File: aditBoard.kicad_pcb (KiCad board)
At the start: 4 copper layers, 13.2 x 30 mm, 31 parts, among them J1 USB_C_Receptacle_USB2.0, J2 Hashboard0, U2 W25X40CLUXIG TR, U3 RP2040, U4 AP2112K-3.3TRG1, Y1 12MHz

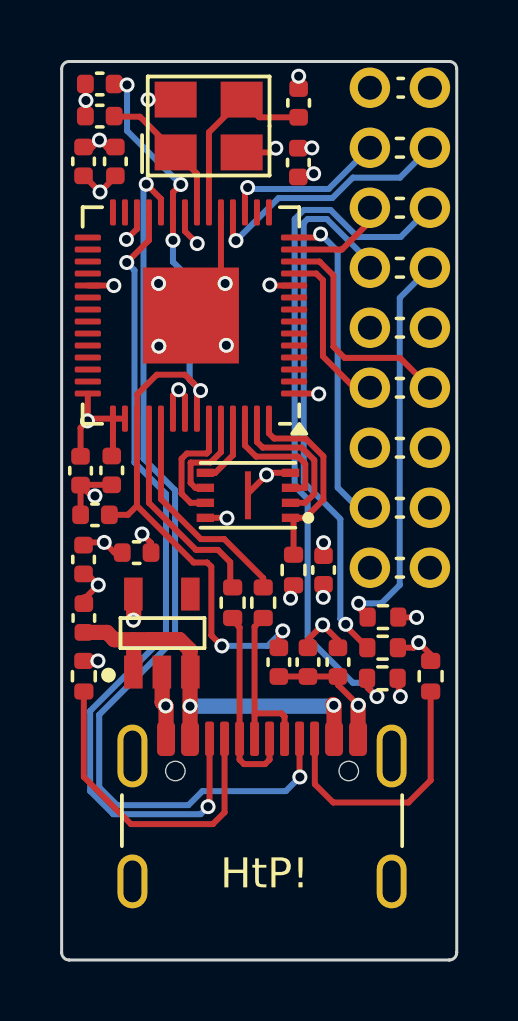
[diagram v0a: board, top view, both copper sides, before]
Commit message: bumped version to 2. added RGB LED
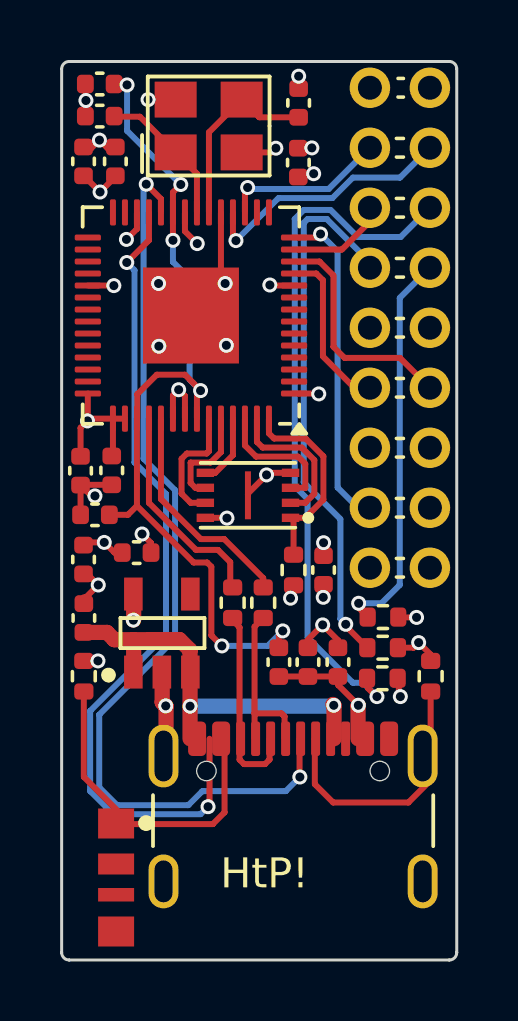
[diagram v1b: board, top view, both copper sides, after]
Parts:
- added U1: SK6812, aditBoard:LED-SMD_4P-L4.0-W1.6-L, F.Cu at (116.2, 108.0)
- U2: value W25X40CLUXIG TR -> W25Q16JVUXIQ
- moved J1 1.03 mm to (122.1, 107.1)
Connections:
- U3 pad 3: unconnected-(U3-GPIO1-Pad3) -> Net-(U1-DIN)
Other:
- copper layers 4 -> 6
- board text added: "v2"
- board text removed: "v1"

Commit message: switched to 6L. Routed LED
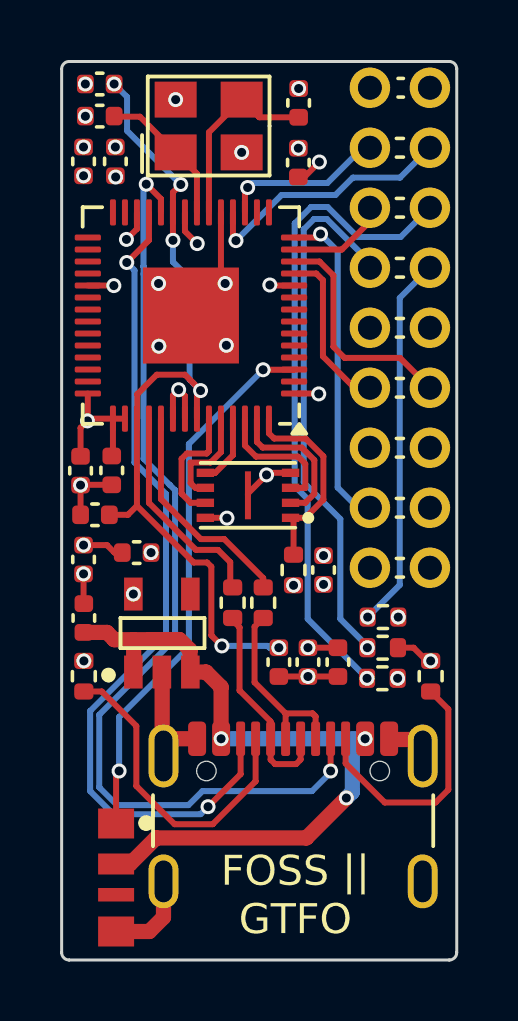
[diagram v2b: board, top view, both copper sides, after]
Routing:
- net Net-(U1-DIN): track 0.00 -> 18.2 mm, vias 0 -> 2
- net /5V: track 13.9 -> 24.3 mm, vias 2 -> 3
- net /GND: track 26.3 -> 19.6 mm, vias 21 -> 22
- net /3V3: track 19.4 -> 16.1 mm, vias 15 -> 16
- net /A2: track 23.4 -> 21.8 mm
- net /1V1: track 29.2 -> 28.0 mm
- net /SWCLK: track 31.4 -> 32.3 mm
- net /A0: track 13.2 -> 12.5 mm
- net Net-(J1-CC2): track 8.90 -> 8.24 mm
- added copper zone on In3.Cu, net /3V3
- added copper zone on In4.Cu, net /GND
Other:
- board text added: "FOSS || GTFO"
- board text removed: "HtP!"

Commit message: Added option for BOOT and RESET buttons. added gerbers and BOM
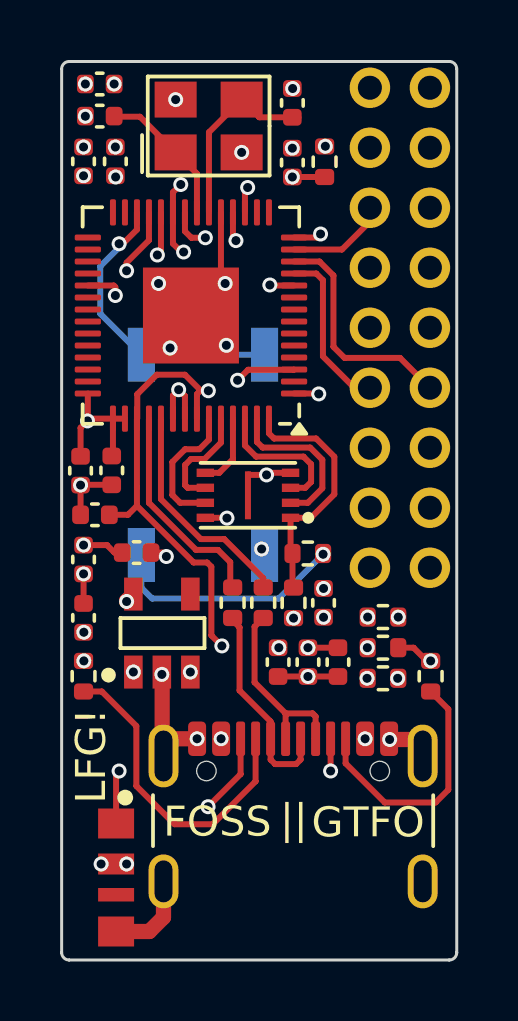
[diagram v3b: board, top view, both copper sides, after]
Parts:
- added R6: 1k, Resistor_SMD:R_0402_1005Metric, F.Cu at (122.6, 97.2)
- added R7: 49.9k, Resistor_SMD:R_0402_1005Metric, F.Cu at (123.1, 84.2)
- added SW2: GT-TC029B-H025-L1N, aditBoard:SW_CS1213AGF260_CRS, B.Cu at (119.1, 97.3)
- added SW3: GT-TC029B-H025-L1N, aditBoard:SW_CS1213AGF260_CRS, B.Cu at (119.1, 90.6)
- moved C15 1.09 mm to (123.1, 98.9)
- moved R1 1.09 mm to (122.1, 98.9)
- moved C4 0.21 mm to (122.0, 82.2)
- moved C12 0.20 mm to (122.0, 84.2)
- moved G*** 0.05 mm to (119.8, 95.7)
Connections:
- U3 pad 26: /3V3 -> Net-(U3-RUN)
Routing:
- net /5V: track 24.3 -> 0.88 mm, vias 3 -> 7
- net Net-(U3-RUN): track 0.00 -> 14.5 mm, vias 0 -> 2
- net Net-(R6-Pad2): track 0.00 -> 7.94 mm, vias 0 -> 1
- net /SWCLK: track 32.3 -> 30.0 mm
- net /GND: track 19.6 -> 21.7 mm, vias 22 -> 26
- net /QSPI_SS: track 6.68 -> 8.40 mm
- net /1V1: track 28.0 -> 29.4 mm
- net Net-(U1-DIN): track 18.2 -> 19.2 mm
- net /3V3: vias 16 -> 15
- added copper zone on In2.Cu, net /5V
- removed copper zone on In2.Cu, net /3V3
- removed copper zone on In4.Cu, net /GND
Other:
- board text added: "FOSS"
- board text added: "GTFO"
- board text added: "LFG!"
- board text added: "||"
- board text removed: "FOSS || GTFO"
